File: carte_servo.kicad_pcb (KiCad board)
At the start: 4 copper layers, 48.4 x 99.2 mm, 138 parts, among them J10 Conn_01x03_Male, J11 Transistor_2, J12 Transistor_1, J13 Transistor_4, J14 Transistor_.3, J16 Conn_01x04_Male, J17 Conn_01x04_Male, J18 Conn_01x03_Male, J19 Conn_01x03_Male, J2 Conn_02x04_Top_Bottom, J20 Stepper, J21 Stepper, J24 Conn_LEDs, J25 Conn_AX12, J29 Conn_AX12, J5 Conn_01x03_Male, J6 Conn_01x03_Male, J7 Conn_01x03_Male, J8 Conn_01x03_Male, J9 Conn_01x03_Male, P1 USB_C_Plug_USB2.0, Q1 DMN2011UTS, Q2 DMN2011UTS, Q3 DMN2011UTS, Q4 DMN2011UTS, Q6 DMN2011UTS, Q7 CSD17307Q5A, Q8 CSD17579Q5A, SW1 CK_KMS2xxG, U1 XGZP6897D_differential_pressu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, U10 TPS563200, U2 XGZP6897D_differential_pressu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, U3 TMC2208_SILENTSTEPSTICK, U4 TMC2208_SILENTSTEPSTICK, U5 74LVC2G241, U6 SN65HVD230, U7 LD1117S33TR_SOT223, U8 ESP32-S3-WROOM-1, U9 LM3150MH

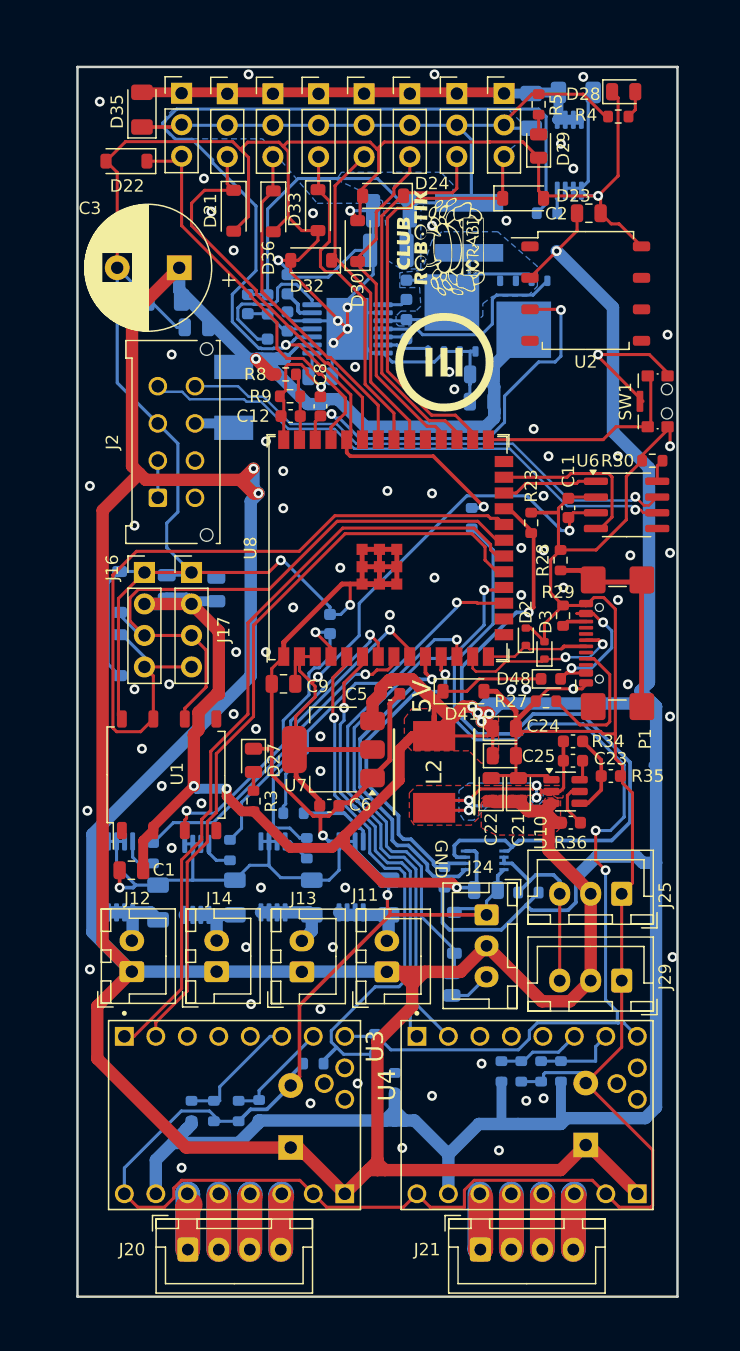
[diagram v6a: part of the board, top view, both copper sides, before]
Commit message: add mounting holes
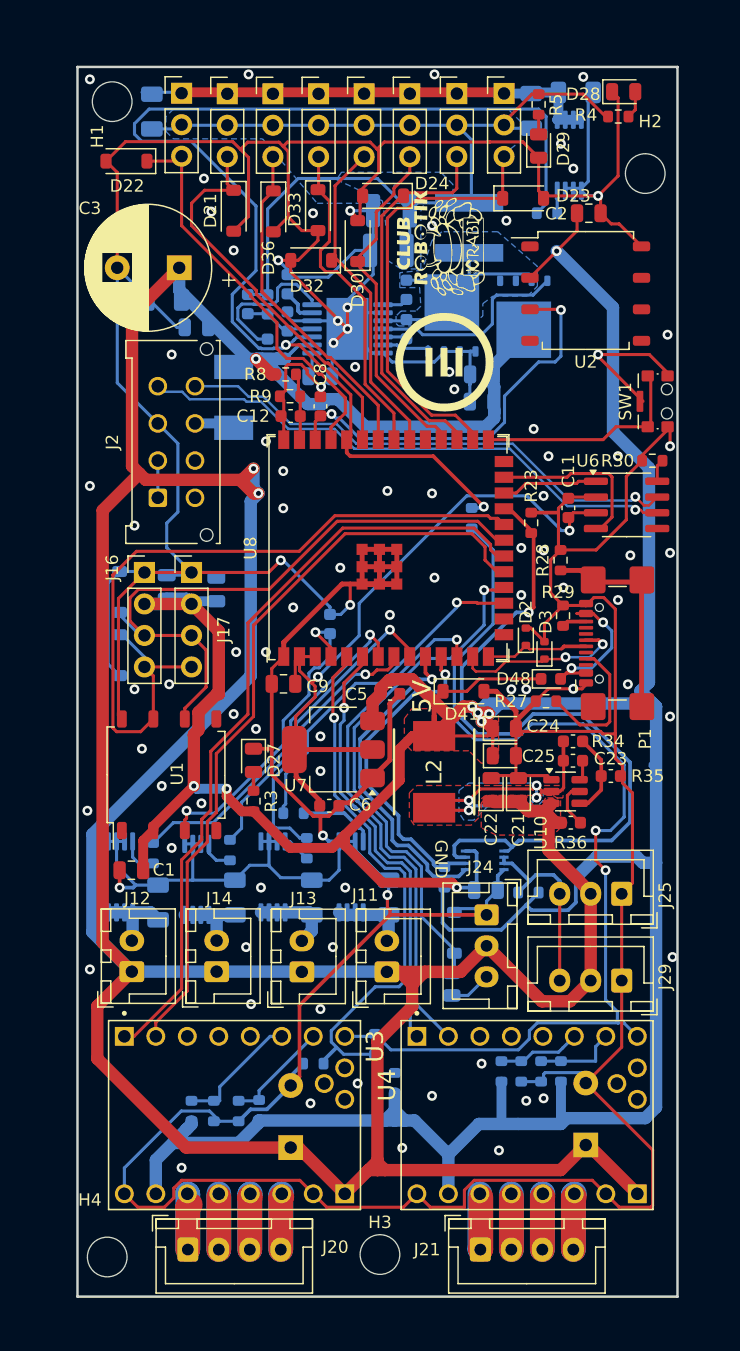
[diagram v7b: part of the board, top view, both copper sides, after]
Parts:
- added H1: MountingHole, MountingHole:MountingHole_3.2mm_M3, F.Cu at (142.4, 64.2)
- added H2: MountingHole, MountingHole:MountingHole_3.2mm_M3, F.Cu at (185.4, 70.0)
- added H3: MountingHole, MountingHole:MountingHole_3.2mm_M3, F.Cu at (164.0, 157.2)
- added H4: MountingHole, MountingHole:MountingHole_3.2mm_M3, F.Cu at (142.0, 157.4)
- D35: moved to B.Cu
- moved D35 0.81 mm to (145.6, 65.0)
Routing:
- net ENABLE_SERVO_POWER_1: track 93.8 -> 98.5 mm
- net /ServoDCDC/VOUT: track 79.4 -> 78.6 mm

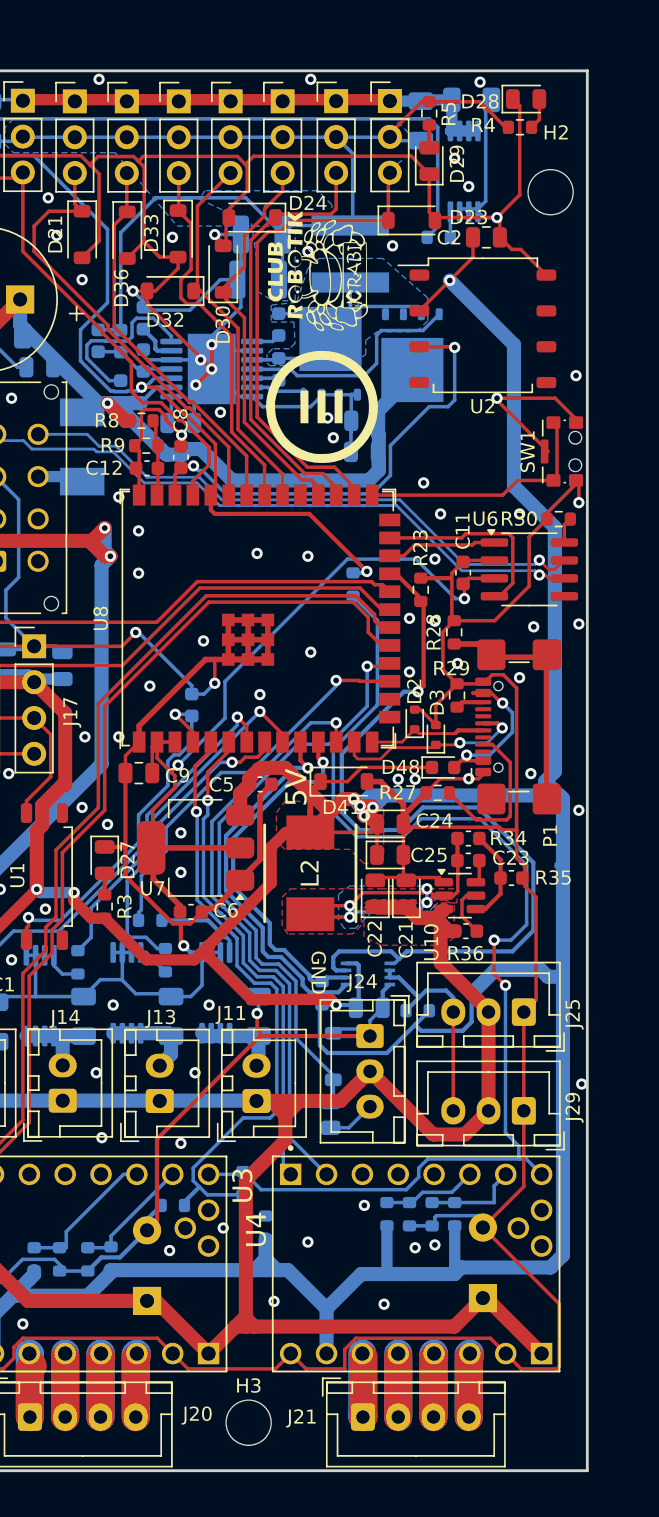
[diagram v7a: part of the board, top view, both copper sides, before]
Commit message: add power status LEDs
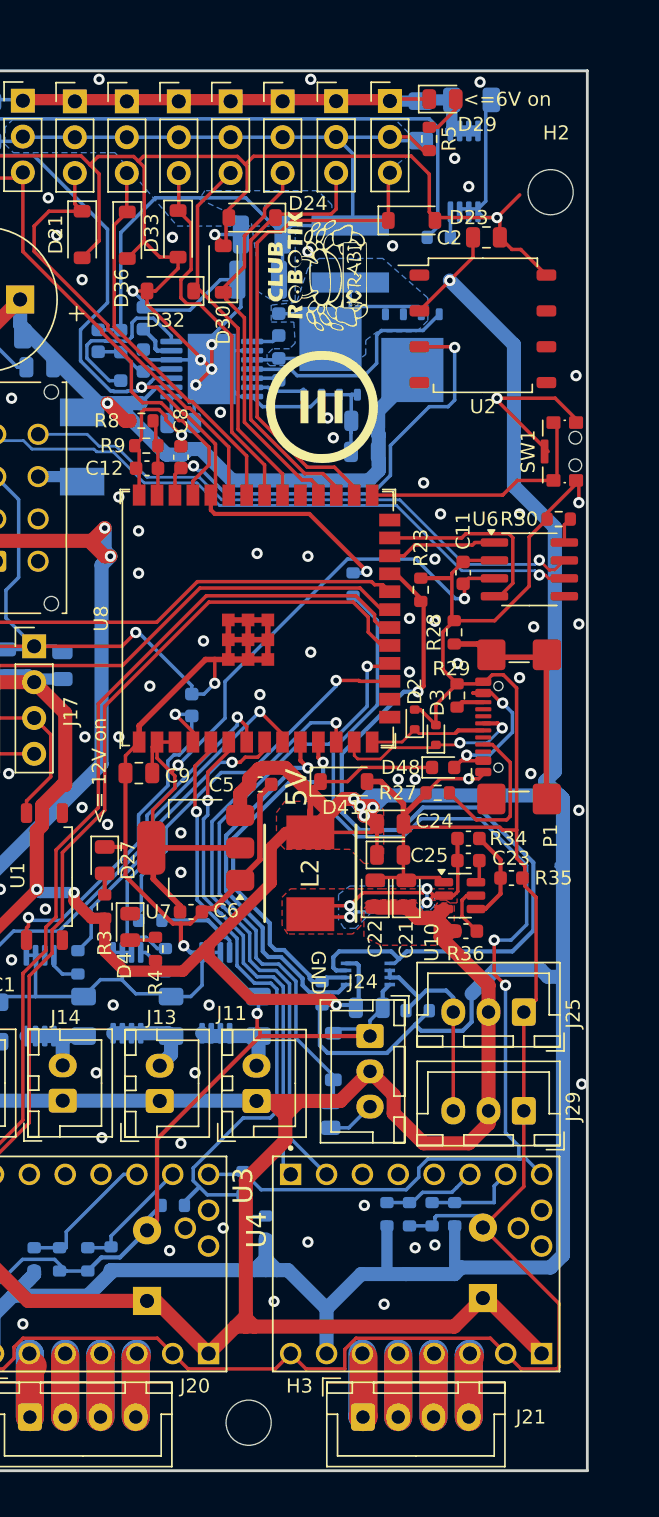
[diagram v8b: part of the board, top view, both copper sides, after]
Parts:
- removed D28: LED_Small, LED_SMD:LED_0805_2012Metric
- added D4: LED_Small, LED_SMD:LED_0805_2012Metric, F.Cu at (155.6, 122.1)
- moved R4 63.7 mm to (157.4, 123.6), turned to -90 degrees
- moved D29 4.48 mm to (177.7, 63.4), turned to 0 degrees
- moved R5 1.80 mm to (176.8, 66.2), turned to -90 degrees
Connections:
- D29 pad 1: GND -> /Servos/GND_SERVO_2
- R4 pad 2: /ServoDCDC/VOUT -> 5V
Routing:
- net /ServoDCDC/VOUT: track 78.6 -> 71.6 mm
- net GND: track 617.9 -> 610.9 mm
- net /Servos/GND_SERVO_2: track 37.9 -> 40.8 mm
- net 5V: track 308.9 -> 310.9 mm
- net BATT_12V: track 313.6 -> 315.4 mm
- net Net-(D29-A): track 1.60 -> 3.13 mm
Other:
- board text added: "<= 12V on"
- board text added: "<=6V on"
